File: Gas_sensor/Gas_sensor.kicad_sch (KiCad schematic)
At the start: 143 parts, among them J1 Conn_02x02_Counter_Clockwise, J2 Conn_01x04, J3 Conn_01x10, J4 Conn_01x01, J5 Conn_01x01, Q1 DMC1229UFDB, Q2 DMC1229UFDB, Q3 Q_NMOS_GSD, Q4 Q_NMOS_GSD, Q5 Q_NMOS_GSD, Q6 Q_NMOS_GSD, SW1 SW_Push, SW10 SW_Push, SW11 SW_Push, SW12 SW_Push, SW2 SW_Push, SW3 SW_Push, SW4 SW_Push, SW5 SW_Push, SW6 SW_Push, SW7 SW_Push, SW8 SW_Push, SW9 SW_Push, U1 LPV511, U10 MCP1700-3302E_SOT23, U11 STM32F401CCUx, U12 TMP117, U13 TPS63070, U14 TPS79333-EP, U15 REG102GA, U2 LPV511, U3 MCP47CMB22, U4 MCP6V71, U5 LPV511, U6 MCP6V71, U7 MCP6V71, U8 MCP6V71, U9 ADS1115IDGS, Y1 25MHz

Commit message: gas sensor : update layout
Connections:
- net at U3.5 (Vout1): now also R7.1

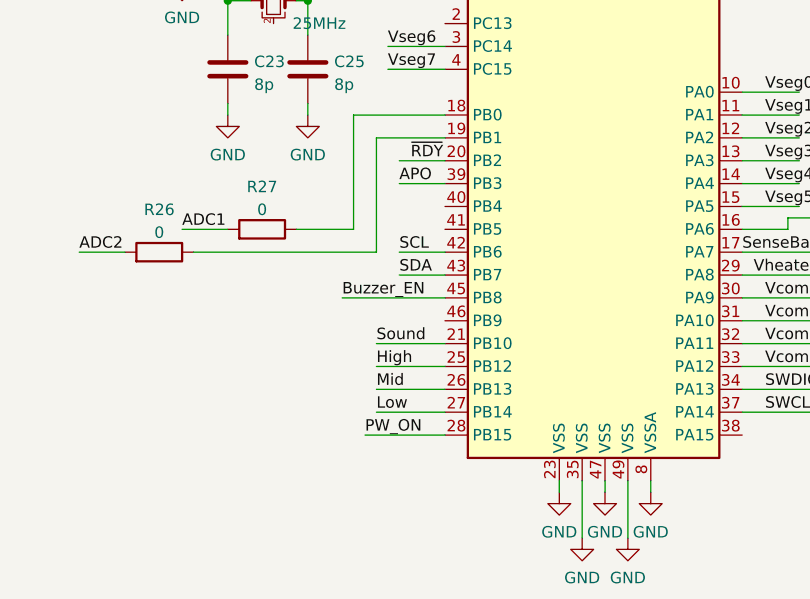
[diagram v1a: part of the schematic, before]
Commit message: gas sensor : update layout, power missing
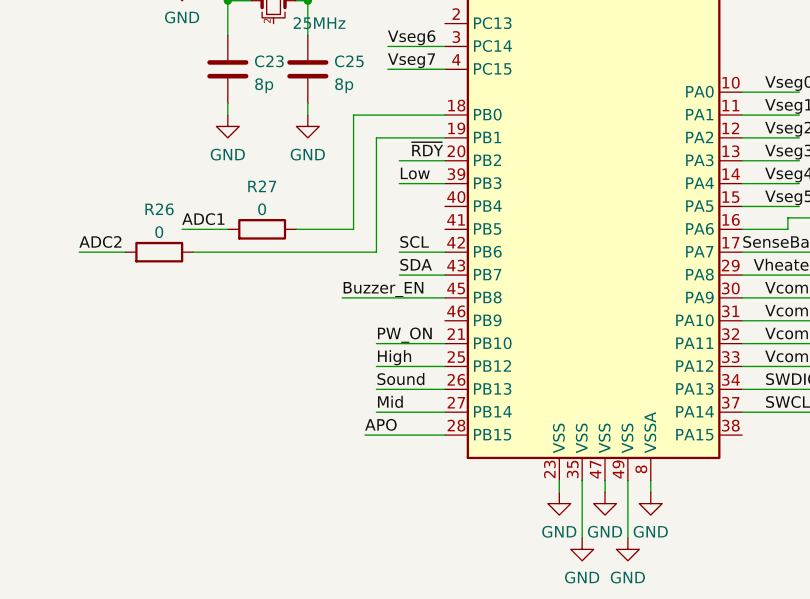
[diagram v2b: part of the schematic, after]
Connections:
- net APO: now also U11.28 (PB15); no longer U11.39 (PB3)
- net Low: now also U11.39 (PB3); no longer U11.27 (PB14)
- net Mid: now also U11.27 (PB14); no longer U11.26 (PB13)
- net PW_ON: now also U11.21 (PB10); no longer U11.28 (PB15)
- net Sound: now also U11.26 (PB13); no longer U11.21 (PB10)
- net at U3.5 (Vout1): now also R7.1
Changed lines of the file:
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@@
+    (effects (font (size 1.27 1.27)) (justify left bottom))
+  )
+  (label "Sound" (at 346.71 245.11 0)
     (effects (font (size 1.27 1.27)) (justify left bottom))
   )
@@
     (effects (font (size 1.27 1.27)) (justify left bottom))
   )
+  (label "Low" (at 349.25 222.25 0)
+    (effects (font (size 1.27 1.27)) (justify left bottom))
+  )
   (label "ADC0" (at 242.57 318.77 0)
     (effects (font (size 1.27 1.27)) (justify left bottom))
   )
-  (label "Low" (at 346.71 247.65 0)
-    (effects (font (size 1.27 1.27)) (justify left bottom))
-  )
   (label "Vheater_EN" (at 248.92 207.01 0)
     (effects (font (size 1.27 1.27)) (justify left bottom))
   )
-  (label "Mid" (at 346.71 245.11 0)
+  (label "Mid" (at 346.71 247.65 0)
     (effects (font (size 1.27 1.27)) (justify left bottom))
   )
@@
     (effects (font (size 1.27 1.27)) (justify left bottom))
   )
-  (label "Sound" (at 346.71 240.03 0)
-    (effects (font (size 1.27 1.27)) (justify left bottom))
-  )
   (label "~{RDY}" (at 307.34 339.09 0)
     (effects (font (size 1.27 1.27)) (justify left bottom))
@@
     (effects (font (size 1.27 1.27)) (justify left bottom))
   )
-  (label "APO" (at 349.25 222.25 0)
-    (effects (font (size 1.27 1.27)) (justify left bottom))
-  )
   (label "SCL" (at 107.95 321.31 0)
     (effects (font (size 1.27 1.27)) (justify left bottom))
@@
     (effects (font (size 1.27 1.27)) (justify left bottom))
   )
+  (label "PW_ON" (at 346.71 240.03 0)
+    (effects (font (size 1.27 1.27)) (justify left bottom))
+  )
   (label "Vseg2" (at 453.39 232.41 0)
     (effects (font (size 1.27 1.27)) (justify left bottom))
@@
     (effects (font (size 1.27 1.27)) (justify left bottom))
   )
+  (label "APO" (at 345.44 250.19 0)
+    (effects (font (size 1.27 1.27)) (justify left bottom))
+  )
   (label "Vseg5" (at 453.39 240.03 0)
     (effects (font (size 1.27 1.27)) (justify left bottom))
@@
     (effects (font (size 1.27 1.27)) (justify left bottom))
   )
-  (label "PW_ON" (at 345.44 250.19 0)
-    (effects (font (size 1.27 1.27)) (justify left bottom))
-  )

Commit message: Update Gas sensor
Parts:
- R10: value R -> 5
- R21, R23, R27: value 0 -> nc
- R3, R8: value R -> 10k
- R4: value R -> 5k
- R5: value R -> 82k
- R56: value nc -> 0
- R6: value R -> 100k
- R7, R9: value 0 -> 1k
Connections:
- net at U3.5 (Vout1): now also R7.1
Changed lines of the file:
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@@
     (stroke (width 0) (type default) (color 0 0 0 0))
   )
-  (polyline (pts (xy 78.74 109.22) (xy 78.74 53.34))
+  (polyline (pts (xy 78.74 109.22) (xy 78.74 41.91))
     (stroke (width 0) (type default) (color 0 0 0 0))
   )
@@
     (stroke (width 0) (type default) (color 0 0 0 0))
   )
-  (polyline (pts (xy 78.74 53.34) (xy 203.2 53.34))
+  (polyline (pts (xy 78.74 41.91) (xy 203.2 41.91))
     (stroke (width 0) (type default) (color 0 0 0 0))
   )
@@
     (stroke (width 0) (type default) (color 0 0 0 0))
   )
-  (polyline (pts (xy 203.2 53.34) (xy 203.2 109.22))
+  (polyline (pts (xy 203.2 41.91) (xy 203.2 109.22))
     (stroke (width 0) (type default) (color 0 0 0 0))
   )
@@
     (in_bom yes) (on_board yes) (fields_autoplaced)
     (property "Reference" "R27" (id 0) (at 334.01 222.6142 90))
-    (property "Value" "0" (id 1) (at 334.01 225.1511 90))
+    (property "Value" "nc" (id 1) (at 334.01 225.1511 90))
     (property "Footprint" "Yame_library:SM0402-MR" (id 2) (at 334.01 229.108 90)
       (effects (font (size 1.27 1.27)) hide)
@@
       (effects (font (size 1.27 1.27)) (justify right))
     )
-    (property "Value" "nc" (id 1) (at 278.638 359.8422 0)
+    (property "Value" "0" (id 1) (at 278.638 359.8422 0)
       (effects (font (size 1.27 1.27)) (justify right))
     )
@@
       (effects (font (size 1.27 1.27)) (justify left))
     )
-    (property "Value" "R" (id 1) (at 173.228 56.3122 0)
+    (property "Value" "10k" (id 1) (at 173.228 56.3122 0)
       (effects (font (size 1.27 1.27)) (justify left))
     )
@@
       (effects (font (size 1.27 1.27)) (justify left))
     )
-    (property "Value" "R" (id 1) (at 133.858 100.7622 0)
+    (property "Value" "5k" (id 1) (at 133.858 100.7622 0)
       (effects (font (size 1.27 1.27)) (justify left))
     )
@@
       (effects (font (size 1.27 1.27)) (justify left))
     )
-    (property "Value" "R" (id 1) (at 189.738 193.4722 0)
+    (property "Value" "5" (id 1) (at 189.738 193.4722 0)
       (effects (font (size 1.27 1.27)) (justify left))
     )
@@
       (effects (font (size 1.27 1.27)) (justify left))
     )
-    (property "Value" "R" (id 1) (at 150.368 237.9222 0)
+    (property "Value" "100k" (id 1) (at 150.368 237.9222 0)
       (effects (font (size 1.27 1.27)) (justify left))
     )
@@
     (in_bom yes) (on_board yes) (fields_autoplaced)
     (property "Reference" "R23" (id 0) (at 266.7 347.0742 90))
-    (property "Value" "0" (id 1) (at 266.7 349.6111 90))
+    (property "Value" "nc" (id 1) (at 266.7 349.6111 90))
     (property "Footprint" "Yame_library:SM0402-MR" (id 2) (at 266.7 353.568 90)
       (effects (font (size 1.27 1.27)) hide)
@@
     (in_bom yes) (on_board yes) (fields_autoplaced)
     (property "Reference" "R7" (id 0) (at 158.75 317.8642 90))
-    (property "Value" "0" (id 1) (at 158.75 320.4011 90))
+    (property "Value" "1k" (id 1) (at 158.75 320.4011 90))
     (property "Footprint" "Yame_library:SM0402-MR" (id 2) (at 158.75 324.358 90)
       (effects (font (size 1.27 1.27)) hide)
@@
     (in_bom yes) (on_board yes) (fields_autoplaced)
     (property "Reference" "R9" (id 0) (at 173.99 307.7042 90))
-    (property "Value" "0" (id 1) (at 173.99 310.2411 90))
+    (property "Value" "1k" (id 1) (at 173.99 310.2411 90))
     (property "Footprint" "Yame_library:SM0402-MR" (id 2) (at 173.99 314.198 90)
       (effects (font (size 1.27 1.27)) hide)
@@
       (effects (font (size 1.27 1.27)) (justify left))
     )
-    (property "Value" "R" (id 1) (at 150.368 206.1722 0)
+    (property "Value" "82k" (id 1) (at 150.368 206.1722 0)
       (effects (font (size 1.27 1.27)) (justify left))
     )
@@
       (effects (font (size 1.27 1.27)) (justify left))
     )
-    (property "Value" "R" (id 1) (at 133.858 69.0122 0)
+    (property "Value" "10k" (id 1) (at 133.858 69.0122 0)
       (effects (font (size 1.27 1.27)) (justify left))
     )
@@
     (in_bom yes) (on_board yes) (fields_autoplaced)
     (property "Reference" "R21" (id 0) (at 266.7 331.8342 90))
-    (property "Value" "0" (id 1) (at 266.7 334.3711 90))
+    (property "Value" "nc" (id 1) (at 266.7 334.3711 90))
     (property "Footprint" "Yame_library:SM0402-MR" (id 2) (at 266.7 338.328 90)
       (effects (font (size 1.27 1.27)) hide)
@@
     )
     (path "/ea757973-5396-4293-933d-4a0eb1ea315b"
-      (reference "R3") (unit 1) (value "R") (footprint "Yame_library:SM0402-MR")
+      (reference "R3") (unit 1) (value "10k") (footprint "Yame_library:SM0402-MR")
     )
     (path "/401c417f-a4fd-4981-903d-0b6c76dfbc21"
-      (reference "R4") (unit 1) (value "R") (footprint "Yame_library:SM0402-MR")
+      (reference "R4") (unit 1) (value "5k") (footprint "Yame_library:SM0402-MR")
     )
     (path "/b1acc487-8c31-44b8-8141-cbb707eb4b83"
-      (reference "R5") (unit 1) (value "R") (footprint "Yame_library:SM0402-MR")
+      (reference "R5") (unit 1) (value "82k") (footprint "Yame_library:SM0402-MR")
     )
     (path "/7b5e60d3-74ce-427f-80eb-ff5f80797da9"
-      (reference "R6") (unit 1) (value "R") (footprint "Yame_library:SM0402-MR")
+      (reference "R6") (unit 1) (value "100k") (footprint "Yame_library:SM0402-MR")
     )
     (path "/92aeb820-8538-48bd-9655-ff379b5a94fd"
-      (reference "R7") (unit 1) (value "0") (footprint "Yame_library:SM0402-MR")
+      (reference "R7") (unit 1) (value "1k") (footprint "Yame_library:SM0402-MR")
     )
     (path "/1d3b0084-7831-4735-8900-54cbe3a40b4e"
-      (reference "R8") (unit 1) (value "R") (footprint "Yame_library:SM0402-MR")
+      (reference "R8") (unit 1) (value "10k") (footprint "Yame_library:SM0402-MR")
     )
     (path "/ad9d23cf-3d6f-48af-8628-9b602f8dd009"
-      (reference "R9") (unit 1) (value "0") (footprint "Yame_library:SM0402-MR")
+      (reference "R9") (unit 1) (value "1k") (footprint "Yame_library:SM0402-MR")
     )
     (path "/6bd8c2d2-adf4-4a23-b5b4-93dc16b6f483"
-      (reference "R10") (unit 1) (value "R") (footprint "Yame_library:SM0402-MR")
+      (reference "R10") (unit 1) (value "5") (footprint "Yame_library:SM0402-MR")
     )
     (path "/6431fb1f-2fda-471c-9dd0-dac537f82f81"
@@
     )
     (path "/fcb7fa3a-5eba-4c73-ac04-b6d2c6cea07f"
-      (reference "R21") (unit 1) (value "0") (footprint "Yame_library:SM0402-MR")
+      (reference "R21") (unit 1) (value "nc") (footprint "Yame_library:SM0402-MR")
     )
     (path "/fe2226e1-7a26-4cf5-b8e6-3b1c68bd8455"
@@
     )
     (path "/8595d051-163b-4d5d-a554-58ca85892ff5"
-      (reference "R23") (unit 1) (value "0") (footprint "Yame_library:SM0402-MR")
+      (reference "R23") (unit 1) (value "nc") (footprint "Yame_library:SM0402-MR")
     )
     (path "/a7dcd6a6-2c65-454b-a400-5cfa92f09940"
@@
     )
     (path "/04176f43-7510-48d9-bf36-7bc01c16ee4e"
-      (reference "R27") (unit 1) (value "0") (footprint "Yame_library:SM0402-MR")
+      (reference "R27") (unit 1) (value "nc") (footprint "Yame_library:SM0402-MR")
     )
     (path "/2ed0c814-e666-4cf7-8ddf-d9cfe64d2a68"
@@
     )
     (path "/0951db1c-cb04-4559-aea2-f95b437abd07"
-      (reference "R56") (unit 1) (value "nc") (footprint "Yame_library:SM0402-MR")
+      (reference "R56") (unit 1) (value "0") (footprint "Yame_library:SM0402-MR")
     )
     (path "/179ca6e4-c0d9-4461-b780-9944fb49e0e1"

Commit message: Add X-pressure design
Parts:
- added R?: 100k, Yame_library:SM0201-MR, symbol Device:R
- added R?: 6.2k, Yame_library:SM0201-MR, symbol Device:R
- added R?: 10k, Yame_library:SM0201-MR, symbol Device:R
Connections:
- net +3V3: now also R?.1
- net GND: now also R?.1
- net Vref_DAC: now also R?.1; no longer U1.4 (-)
- net at U1.3 (+), U3.2 (Vref0): now also R?.2
- net at U3.5 (Vout1): now also R7.1
- new net: R?.2, R?.2, U1.4 (-)
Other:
- note added: "ADS1114 address : 1001000"
- note added: "MPC47CMB22 address : 1100000"
- note added: "TMP117 address : 1001001"
